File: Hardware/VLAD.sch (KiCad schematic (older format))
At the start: 5 parts

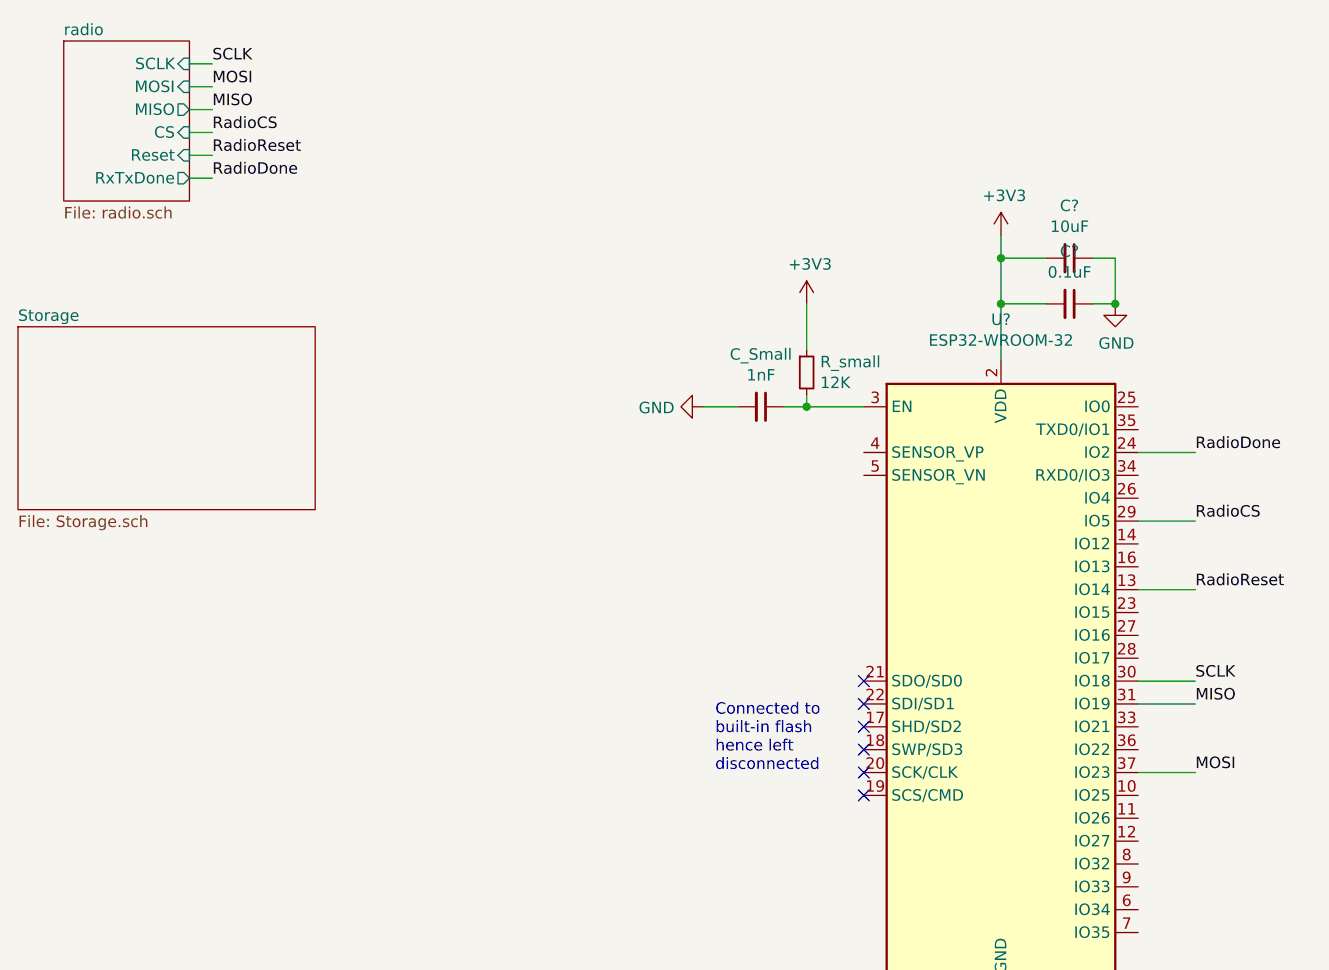
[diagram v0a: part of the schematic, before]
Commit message: Added connections from SD card to ESP32
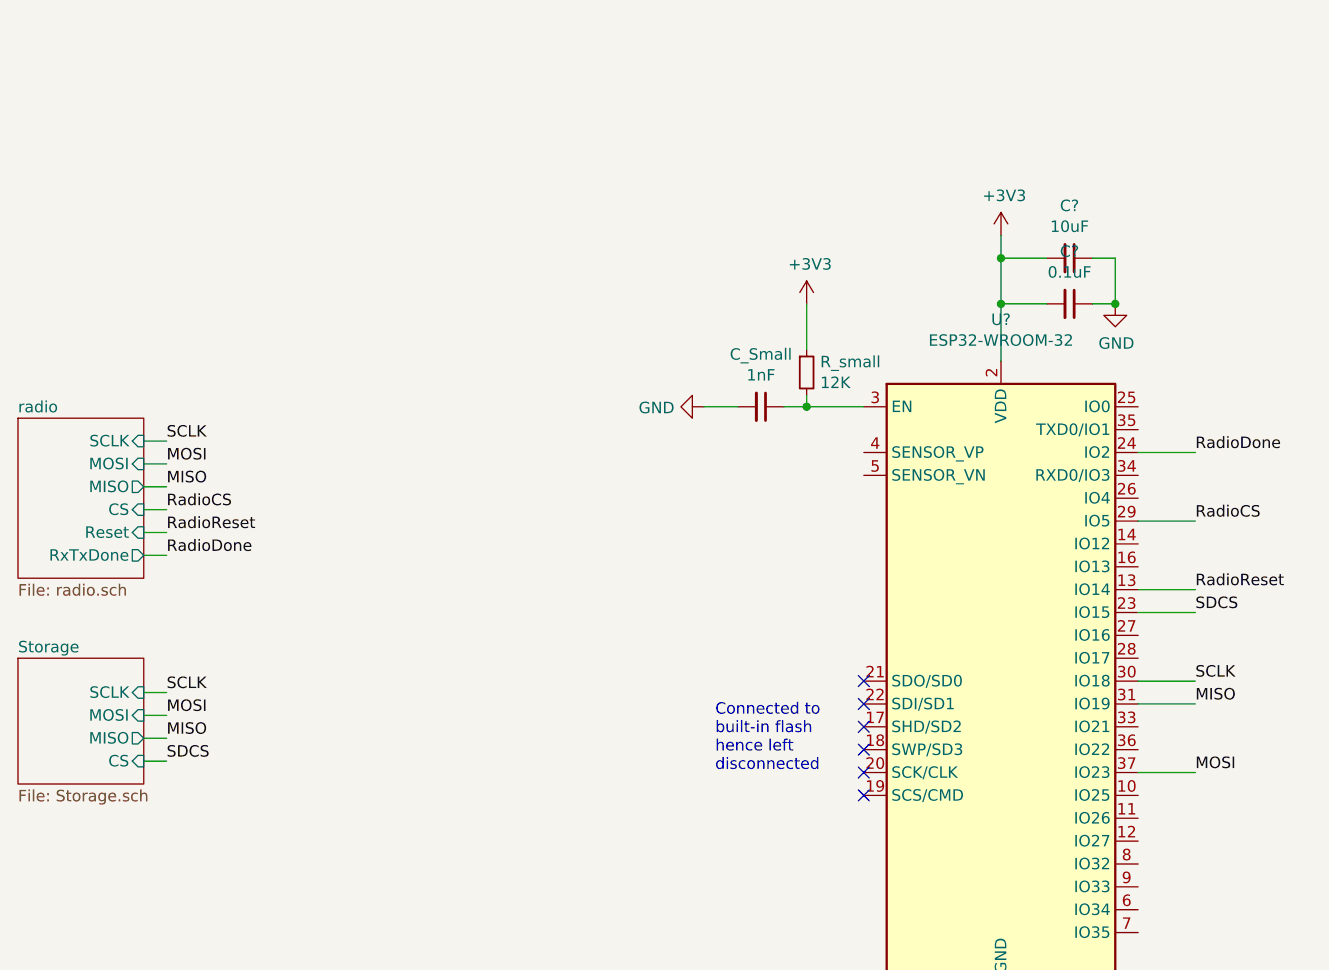
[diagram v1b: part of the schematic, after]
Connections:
- net SDCS: now reaches U?.23 (IO15)
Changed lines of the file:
@@
 	6400 4300 6650 4300
 $Sheet
-S 1500 2350 1300 800
+S 1500 3800 550  550
 U 6068D50F
 F0 "Storage" 50
 F1 "Storage.sch" 50
+F2 "CS" I R 2050 4250 50
+F3 "MOSI" I R 2050 4050 50
+F4 "SCLK" I R 2050 3950 50
+F5 "MISO" O R 2050 4150 50
 $EndSheet
 $Sheet
-S 1700 1100 550  700
+S 1500 2750 550  700
 U 606B714B
 F0 "radio" 50
 F1 "radio.sch" 50
-F2 "MOSI" I R 2250 1300 50
-F3 "MISO" O R 2250 1400 50
-F4 "CS" I R 2250 1500 50
-F5 "Reset" I R 2250 1600 50
-F6 "RxTxDone" O R 2250 1700 50
-F7 "SCLK" I R 2250 1200 50
+F2 "MOSI" I R 2050 2950 50
+F3 "MISO" O R 2050 3050 50
+F4 "CS" I R 2050 3150 50
+F5 "Reset" I R 2050 3250 50
+F6 "RxTxDone" O R 2050 3350 50
+F7 "SCLK" I R 2050 2850 50
 $EndSheet
 Text Label 6650 3900 0    50   ~ 0
@@
 Connection ~ 4950 2700
 Wire Wire Line
-	2250 1200 2350 1200
-Wire Wire Line
-	2250 1300 2350 1300
-Wire Wire Line
-	2250 1400 2350 1400
-Wire Wire Line
-	2250 1500 2350 1500
-Wire Wire Line
-	2250 1600 2350 1600
-Wire Wire Line
-	2250 1700 2350 1700
-Text Label 2350 1200 0    50   ~ 0
+	2050 2850 2150 2850
+Wire Wire Line
+	2050 2950 2150 2950
+Wire Wire Line
+	2050 3050 2150 3050
+Wire Wire Line
+	2050 3150 2150 3150
+Wire Wire Line
+	2050 3250 2150 3250
+Wire Wire Line
+	2050 3350 2150 3350
+Text Label 2150 2850 0    50   ~ 0
 SCLK
-Text Label 2350 1400 0    50   ~ 0
+Text Label 2150 3050 0    50   ~ 0
 MISO
-Text Label 2350 1300 0    50   ~ 0
+Text Label 2150 2950 0    50   ~ 0
 MOSI
 Wire Wire Line
@@
 Text Label 6650 2900 0    50   ~ 0
 RadioDone
-Text Label 2350 1700 0    50   ~ 0
+Text Label 2150 3350 0    50   ~ 0
 RadioDone
 Wire Wire Line
@@
 Text Label 6650 3200 0    50   ~ 0
 RadioCS
-Text Label 2350 1600 0    50   ~ 0
+Text Label 2150 3250 0    50   ~ 0
 RadioReset
-Text Label 2350 1500 0    50   ~ 0
+Text Label 2150 3150 0    50   ~ 0
 RadioCS
 NoConn ~ 5200 3900
@@
 Text Notes 4550 4300 0    50   ~ 0
 Connected to\nbuilt-in flash\nhence left\ndisconnected
+Wire Wire Line
+	2050 3950 2150 3950
+Wire Wire Line
+	2050 4050 2150 4050
+Wire Wire Line
+	2050 4150 2150 4150
+Wire Wire Line
+	2050 4250 2150 4250
+Text Label 2150 3950 0    50   ~ 0
+SCLK
+Text Label 2150 4050 0    50   ~ 0
+MOSI
+Text Label 2150 4150 0    50   ~ 0
+MISO
+Text Label 2150 4250 0    50   ~ 0
+SDCS
+Wire Wire Line
+	6400 3600 6650 3600
+Text Label 6650 3600 0    50   ~ 0
+SDCS
 $EndSCHEMATC

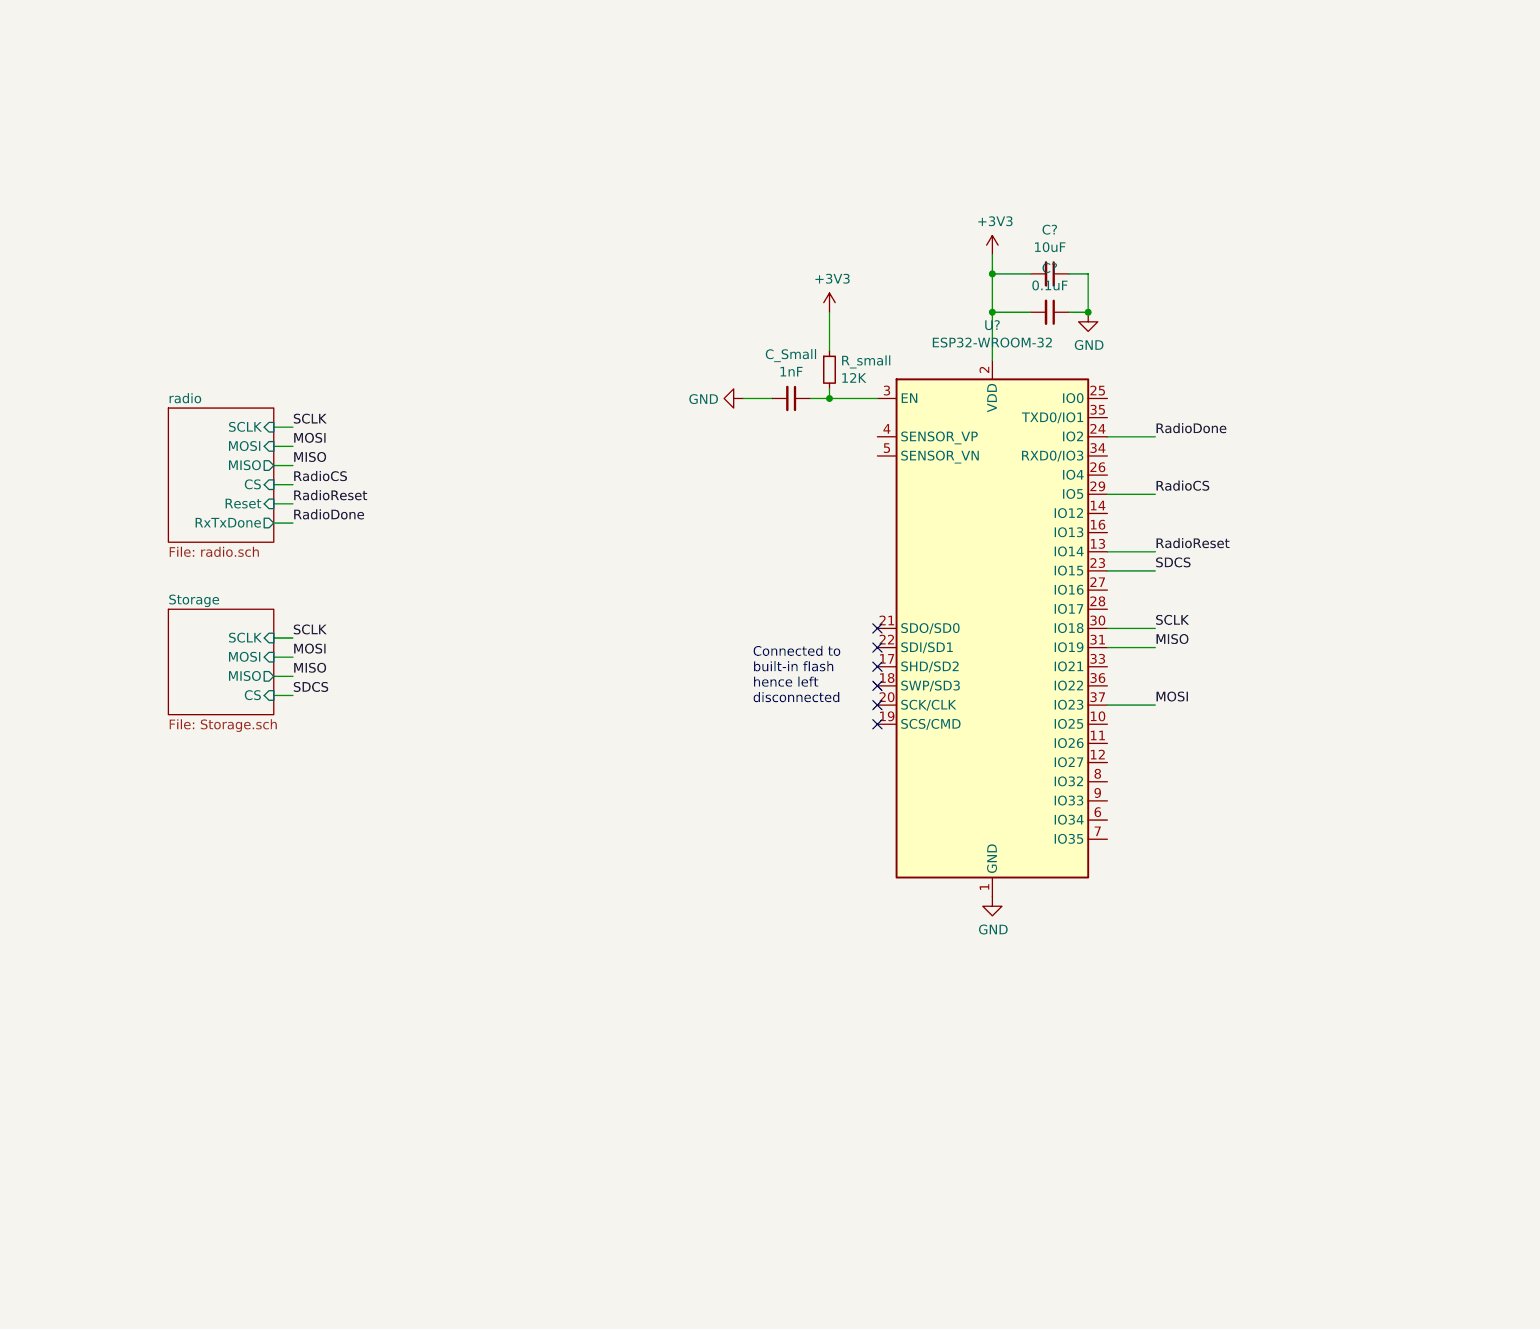
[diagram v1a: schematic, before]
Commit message: Added USB circuitry
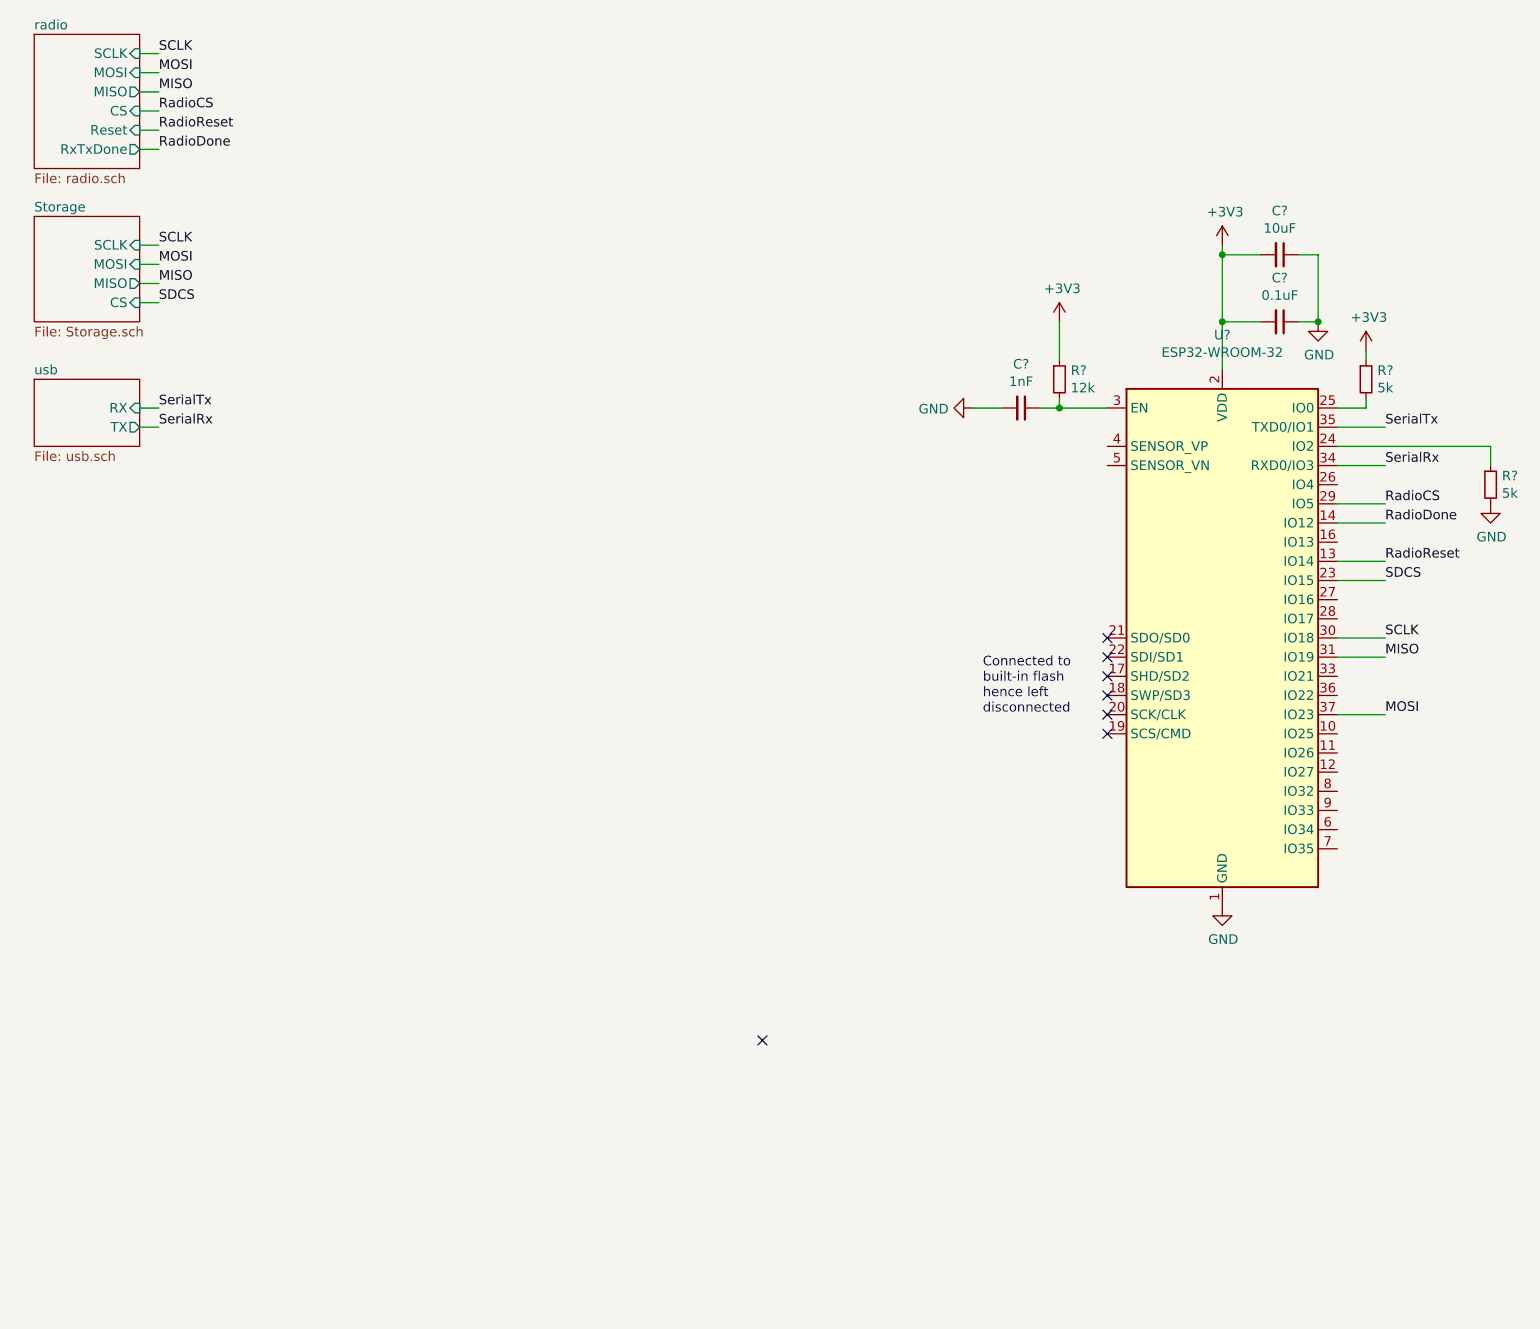
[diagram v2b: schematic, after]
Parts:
- added R? (x2): 5k, symbol Device:R_Small
- R?: renamed from R_small; value 12K -> 12k
- renumbered C_Small to C?
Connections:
- net +3V3: now also R?.1
- net GND: now also R?.2
- net RadioDone: now also U?.14 (IO12); no longer U?.24 (IO2)
- net at U?.25 (IO0): now also R?.2
- net SerialRx: now reaches U?.34 (RXD0/IO3)
- net SerialTx: now reaches U?.35 (TXD0/IO1)
- new net: R?.1, U?.24 (IO2)
- no-connect marks 6 -> 7
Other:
- moved on the sheet: C?, R?, U?

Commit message: Added circuitry to program ESP32
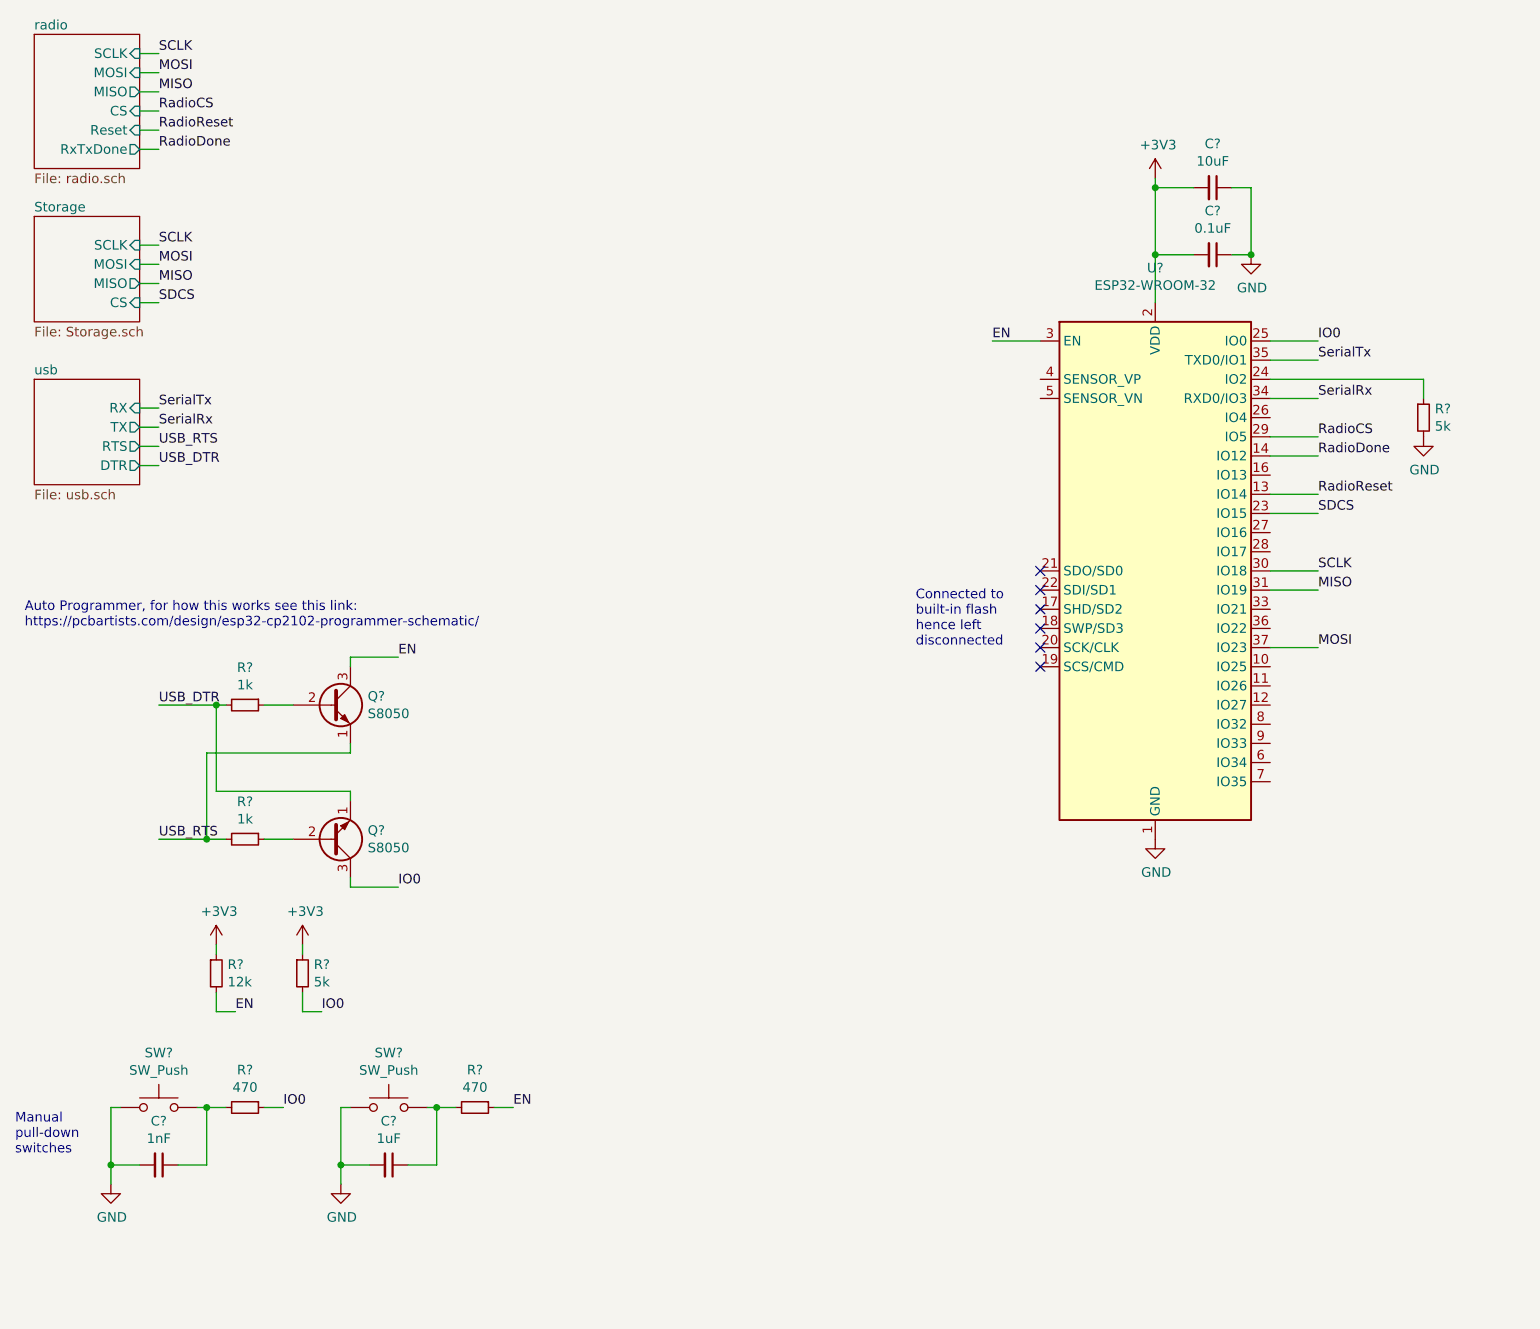
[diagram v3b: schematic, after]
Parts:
- removed C?: 1nF, symbol Device:C_Small
- added C?: 1nF, symbol Device:C_Small
- added C?: 1uF, symbol Device:C_Small
- added Q? (x2): S8050, Package_TO_SOT_THT:TO-92_Inline, symbol Transistor_BJT:S8050
- added R? (x2): 1k, symbol Device:R_Small
- added R? (x2): 470, symbol Device:R_Small
- added SW? (x2): SW_Push, symbol Switch:SW_Push
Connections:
- net GND: now also C?.2, C?.2, SW?.1, SW?.1
- net IO0: now reaches R?.2, U?.25 (IO0)
- net IO0: now also Q?.3 (C), R?.1
- net EN: now reaches R?.2, U?.3 (EN)
- net EN: now also Q?.3 (C), R?.1
- new net: Q?.2 (B), R?.1 (x2)
- new net: C?.1, R?.2, SW?.2 (x2)
- new net USB_DTR: Q?.1 (E), R?.2
- new net USB_RTS: Q?.1 (E), R?.2
- no-connect marks 7 -> 6
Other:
- note added: "Auto Programmer, for how this works see this link:\nhttps://pcbartists.com/design/esp32-cp2102-programmer-schematic/"
- note added: "Manual\npull-down\nswitches"
- moved on the sheet: C?, R?, U?
